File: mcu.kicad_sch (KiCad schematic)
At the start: 1 part, among them U2 ESP32-S3-WROOM-1

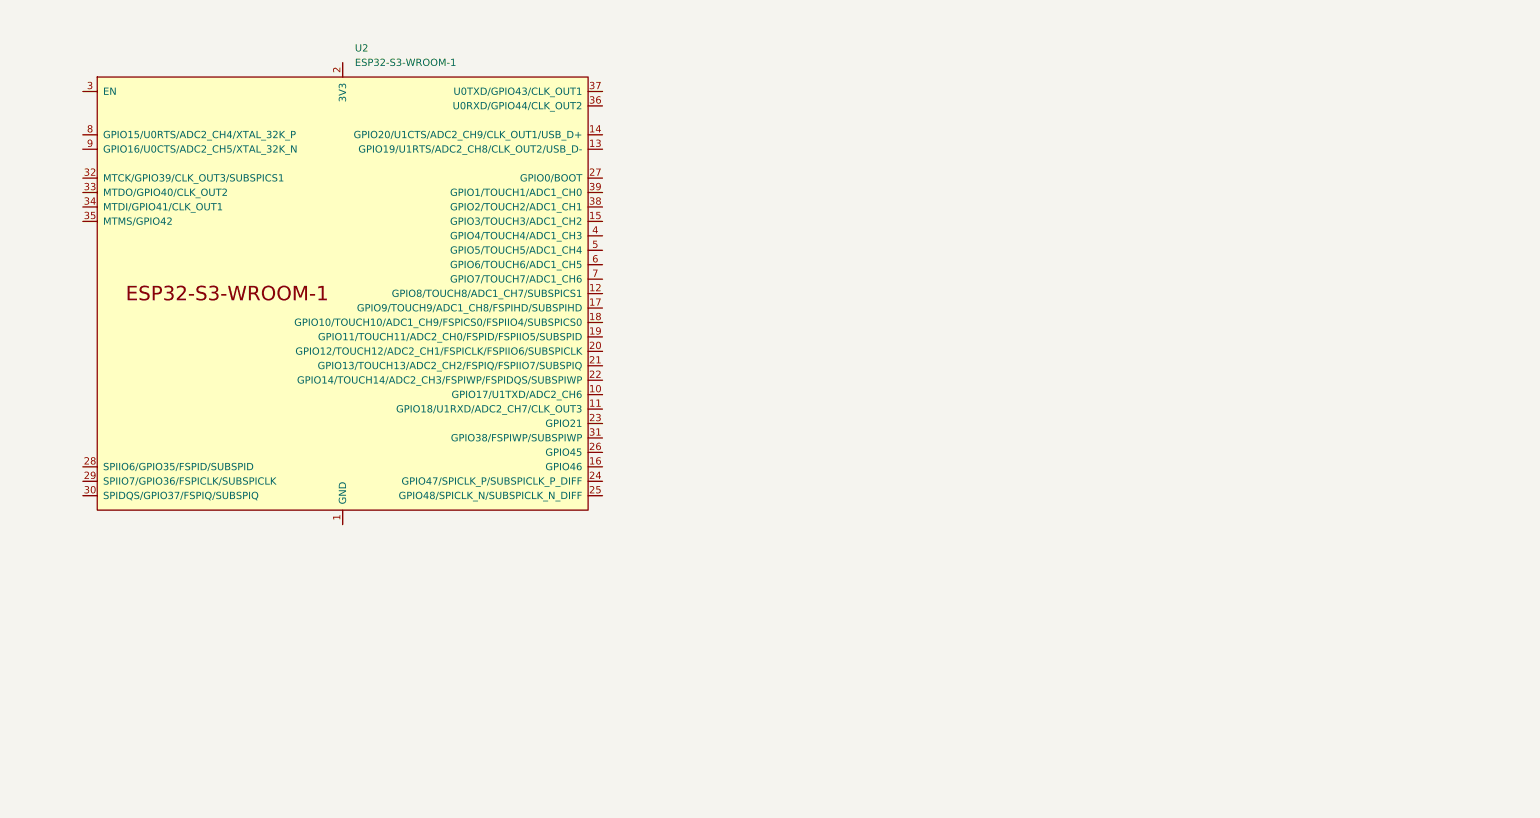
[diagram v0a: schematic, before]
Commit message: power sch. done, MCU powering as well
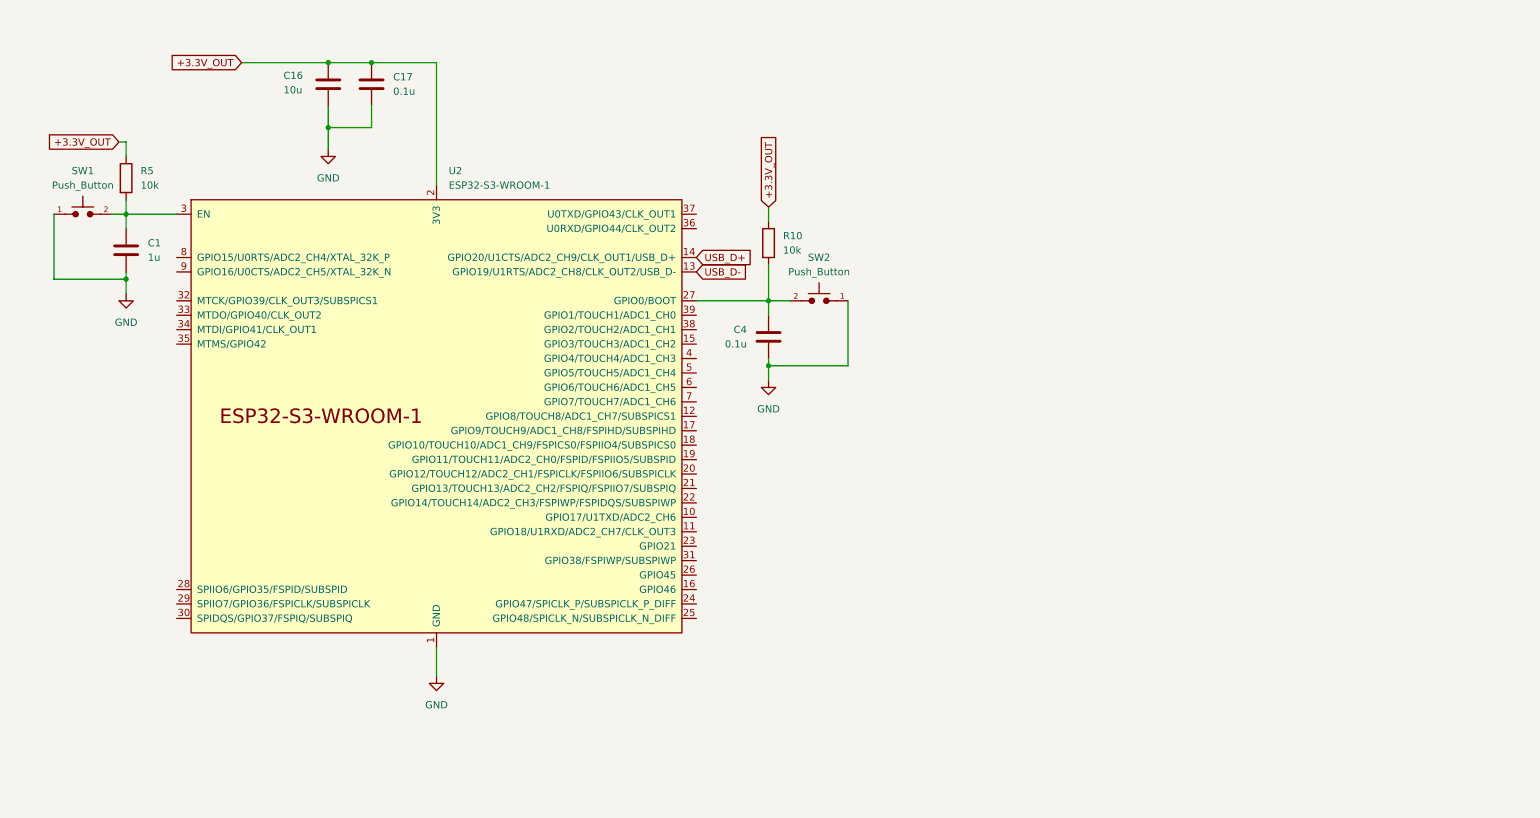
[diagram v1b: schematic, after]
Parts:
- added C1: 1u, symbol Device:C
- added C16: 10u, Capacitor_THT:C_Radial_D12.5mm_H25.0mm_P5.00mm, symbol Device:C
- added C17: 0.1u, Capacitor_THT:C_Radial_D12.5mm_H25.0mm_P5.00mm, symbol Device:C
- added C4: 0.1u, symbol Device:C
- added R10, R5: 10k, symbol Device:R
- added SW1, SW2: Push_Button, Button_Switch_THT:SW_PUSH_6mm, symbol PCM_SL_Devices:Push_Button
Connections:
- net GND: now reaches U2.1 (GND), U2.40 (GND), U2.41 (GND)
- net GND: now also C1.2, C16.2, C17.2, C4.2, SW1.1, SW2.1
- net USB_D-: now reaches U2.13 (GPIO19/U1RTS/ADC2_CH8/CLK_OUT2/USB_D-)
- net USB_D+: now reaches U2.14 (GPIO20/U1CTS/ADC2_CH9/CLK_OUT1/USB_D+)
- net +3.3V_OUT: now reaches U2.2 (3V3)
- net +3.3V_OUT: now also C16.1, C17.1, R10.1, R5.1
- net at U2.27 (GPIO0/BOOT): now also C4.1, R10.2, SW2.2
- net at U2.3 (EN): now also C1.1, R5.2, SW1.2
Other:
- moved on the sheet: U2

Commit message: Small ammendments
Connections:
- net IMU_CS: now reaches U2.18 (GPIO10/TOUCH10/ADC1_CH9/FSPICS0/FSPIIO4/SUBSPICS0)
- net IMU_MOSI: now reaches U2.19 (GPIO11/TOUCH11/ADC2_CH0/FSPID/FSPIIO5/SUBSPID)
- net IMU_SCK: now reaches U2.20 (GPIO12/TOUCH12/ADC2_CH1/FSPICLK/FSPIIO6/SUBSPICLK)
- net IMU_MISO: now reaches U2.21 (GPIO13/TOUCH13/ADC2_CH2/FSPIQ/FSPIIO7/SUBSPIQ)
- net BARO_CS: now reaches U2.22 (GPIO14/TOUCH14/ADC2_CH3/FSPIWP/FSPIDQS/SUBSPIWP)
- net ADC_C_SENSE: now reaches U2.38 (GPIO2/TOUCH2/ADC1_CH1)
- net ADC_V_SENSE: now reaches U2.39 (GPIO1/TOUCH1/ADC1_CH0)
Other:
- moved on the sheet: C4, R10, SW2
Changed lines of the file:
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@@
 	(paper "A4")
+	(junction
+		(at 156.21 67.31)
+		(diameter 0)
+		(color 0 0 0 0)
+	)
 	(junction
 		(at 76.2 25.4)
@@
 	)
 	(junction
-		(at 146.05 78.74)
+		(at 156.21 78.74)
 		(diameter 0)
 		(color 0 0 0 0)
@@
 	)
 	(junction
-		(at 146.05 67.31)
-		(diameter 0)
-		(color 0 0 0 0)
-	)
-	(junction
 		(at 68.58 36.83)
 		(diameter 0)
@@
 	(wire
 		(pts
+			(xy 146.05 78.74) (xy 146.05 81.28)
+		)
+		(stroke
+			(width 0)
+			(type default)
+		)
+	)
+	(wire
+		(pts
 			(xy 76.2 25.4) (xy 87.63 25.4)
 		)
@@
 	(wire
 		(pts
-			(xy 146.05 67.31) (xy 149.86 67.31)
+			(xy 156.21 67.31) (xy 161.29 67.31)
 		)
 		(stroke
@@
 	(wire
 		(pts
-			(xy 160.02 67.31) (xy 160.02 78.74)
+			(xy 171.45 67.31) (xy 171.45 78.74)
 		)
 		(stroke
@@
 	(wire
 		(pts
-			(xy 146.05 78.74) (xy 160.02 78.74)
+			(xy 146.05 78.74) (xy 156.21 78.74)
 		)
 		(stroke
@@
 	(wire
 		(pts
-			(xy 146.05 67.31) (xy 146.05 69.85)
+			(xy 156.21 67.31) (xy 156.21 69.85)
 		)
 		(stroke
@@
 	(wire
 		(pts
-			(xy 133.35 67.31) (xy 146.05 67.31)
+			(xy 133.35 67.31) (xy 156.21 67.31)
 		)
 		(stroke
@@
 	(wire
 		(pts
+			(xy 156.21 49.53) (xy 156.21 53.34)
+		)
+		(stroke
+			(width 0)
+			(type default)
+		)
+	)
+	(wire
+		(pts
 			(xy 33.02 49.53) (xy 33.02 54.61)
 		)
@@
 	(wire
 		(pts
-			(xy 146.05 50.8) (xy 146.05 53.34)
+			(xy 156.21 78.74) (xy 171.45 78.74)
 		)
 		(stroke
@@
 	(wire
 		(pts
-			(xy 146.05 60.96) (xy 146.05 67.31)
-		)
-		(stroke
-			(width 0)
-			(type default)
-		)
-	)
-	(wire
-		(pts
-			(xy 146.05 77.47) (xy 146.05 81.28)
-		)
-		(stroke
-			(width 0)
-			(type default)
+			(xy 156.21 60.96) (xy 156.21 67.31)
+		)
+		(stroke
+			(width 0)
+			(type default)
+		)
+	)
+	(wire
+		(pts
+			(xy 156.21 77.47) (xy 156.21 78.74)
+		)
+		(stroke
+			(width 0)
+			(type default)
+		)
+	)
+	(global_label "IMU_MOSI"
+		(shape input)
+		(at 133.35 95.25 0)
+		(fields_autoplaced yes)
+		(effects
+			(font
+				(size 1.27 1.27)
+			)
+			(justify left)
+		)
+		(property "Intersheetrefs" "${INTERSHEET_REFS}"
+			(at 145.2857 95.25 0)
+			(hide yes)
+			(show_name no)
+			(do_not_autoplace no)
+			(effects
+				(font
+					(size 1.27 1.27)
+				)
+				(justify left)
+			)
+		)
+	)
+	(global_label "IMU_CS"
+		(shape input)
+		(at 133.35 92.71 0)
+		(fields_autoplaced yes)
+		(effects
+			(font
+				(size 1.27 1.27)
+			)
+			(justify left)
+		)
+		(property "Intersheetrefs" "${INTERSHEET_REFS}"
+			(at 143.169 92.71 0)
+			(hide yes)
+			(show_name no)
+			(do_not_autoplace no)
+			(effects
+				(font
+					(size 1.27 1.27)
+				)
+				(justify left)
+			)
+		)
+	)
+	(global_label "ADC_C_SENSE"
+		(shape input)
+		(at 133.35 72.39 0)
+		(fields_autoplaced yes)
+		(effects
+			(font
+				(size 1.27 1.27)
+			)
+			(justify left)
+		)
+		(property "Intersheetrefs" "${INTERSHEET_REFS}"
+			(at 149.2165 72.39 0)
+			(hide yes)
+			(show_name no)
+			(do_not_autoplace no)
+			(effects
+				(font
+					(size 1.27 1.27)
+				)
+				(justify left)
+			)
 		)
 	)
@@
 		)
 	)
+	(global_label "BARO_CS"
+		(shape input)
+		(at 133.35 102.87 0)
+		(fields_autoplaced yes)
+		(effects
+			(font
+				(size 1.27 1.27)
+			)
+			(justify left)
+		)
+		(property "Intersheetrefs" "${INTERSHEET_REFS}"
+			(at 144.7414 102.87 0)
+			(hide yes)
+			(show_name no)
+			(do_not_autoplace no)
+			(effects
+				(font
+					(size 1.27 1.27)
+				)
+				(justify left)
+			)
+		)
+	)
+	(global_label "IMU_SCK"
+		(shape input)
+		(at 133.35 97.79 0)
+		(fields_autoplaced yes)
+		(effects
+			(font
+				(size 1.27 1.27)
+			)
+			(justify left)
+		)
+		(property "Intersheetrefs" "${INTERSHEET_REFS}"
+			(at 144.439 97.79 0)
+			(hide yes)
+			(show_name no)
+			(do_not_autoplace no)
+			(effects
+				(font
+					(size 1.27 1.27)
+				)
+				(justify left)
+			)
+		)
+	)
 	(global_label "+3.3V_OUT"
 		(shape input)
@@
 		)
 	)
-	(global_label "+3.3V_OUT"
+	(global_label "IMU_MISO"
 		(shape input)
-		(at 146.05 50.8 90)
+		(at 133.35 100.33 0)
 		(fields_autoplaced yes)
 		(effects
@@
 		)
 		(property "Intersheetrefs" "${INTERSHEET_REFS}"
-			(at 146.05 37.5338 90)
+			(at 145.2857 100.33 0)
+			(hide yes)
+			(show_name no)
+			(do_not_autoplace no)
+			(effects
+				(font
+					(size 1.27 1.27)
+				)
+				(justify left)
+			)
+		)
+	)
+	(global_label "+3.3V_OUT"
+		(shape input)
+		(at 156.21 49.53 90)
+		(fields_autoplaced yes)
+		(effects
+			(font
+				(size 1.27 1.27)
+			)
+			(justify left)
+		)
+		(property "Intersheetrefs" "${INTERSHEET_REFS}"
+			(at 156.21 36.2638 90)
+			(hide yes)
+			(show_name no)
+			(do_not_autoplace no)
+			(effects
+				(font
+					(size 1.27 1.27)
+				)
+				(justify left)
+			)
+		)
+	)
+	(global_label "ADC_V_SENSE"
+		(shape input)
+		(at 133.35 69.85 0)
+		(fields_autoplaced yes)
+		(effects
+			(font
+				(size 1.27 1.27)
+			)
+			(justify left)
+		)
+		(property "Intersheetrefs" "${INTERSHEET_REFS}"
+			(at 149.0351 69.85 0)
 			(hide yes)
 			(show_name no)
@@
 	(symbol
 		(lib_id "PCM_SL_Devices:Push_Button")
-		(at 154.94 67.31 0)
+		(at 166.37 67.31 0)
 		(mirror y)
 		(unit 1)
@@
 		(fields_autoplaced yes)
 		(property "Reference" "SW2"
-			(at 154.94 59.69 0)
+			(at 166.37 59.69 0)
 			(show_name no)
 			(do_not_autoplace no)
@@
 		)
 		(property "Value" "Push_Button"
-			(at 154.94 62.23 0)
+			(at 166.37 62.23 0)
 			(show_name no)
 			(do_not_autoplace no)
@@
 		)
 		(property "Footprint" "Button_Switch_THT:SW_PUSH_6mm"
-			(at 155.067 70.485 0)
+			(at 166.497 70.485 0)
 			(hide yes)
 			(show_name no)
@@
 		)
 		(property "Datasheet" ""
-			(at 154.94 67.31 0)
+			(at 166.37 67.31 0)
 			(hide yes)
 			(show_name no)
@@
 		)
 		(property "Description" "Common 6mmx6mm Push Button"
-			(at 154.94 67.31 0)
+			(at 166.37 67.31 0)
 			(hide yes)
 			(show_name no)
@@
 	(symbol
 		(lib_id "Device:C")
-		(at 146.05 73.66 0)
+		(at 156.21 73.66 0)
 		(mirror y)
 		(unit 1)
@@
 		(fields_autoplaced yes)
 		(property "Reference" "C4"
-			(at 142.24 72.3899 0)
+			(at 152.4 72.3899 0)
 			(show_name no)
 			(do_not_autoplace no)
@@
 		)
 		(property "Value" "0.1u"
-			(at 142.24 74.9299 0)
+			(at 152.4 74.9299 0)
 			(show_name no)
 			(do_not_autoplace no)
@@
 		)
 		(property "Footprint" ""
-			(at 145.0848 77.47 0)
+			(at 155.2448 77.47 0)
 			(hide yes)
 			(show_name no)
@@
 		)
 		(property "Datasheet" ""
-			(at 146.05 73.66 0)
+			(at 156.21 73.66 0)
 			(hide yes)
 			(show_name no)
@@
 		)
 		(property "Description" "Unpolarized capacitor"
-			(at 146.05 73.66 0)
+			(at 156.21 73.66 0)
 			(hide yes)
 			(show_name no)
@@
 	(symbol
 		(lib_id "Device:R")
-		(at 146.05 57.15 0)
+		(at 156.21 57.15 0)
 		(unit 1)
 		(body_style 1)
@@
 		(fields_autoplaced yes)
 		(property "Reference" "R10"
-			(at 148.59 55.8799 0)
+			(at 158.75 55.8799 0)
 			(show_name no)
 			(do_not_autoplace no)
@@
 		)
 		(property "Value" "10k"
-			(at 148.59 58.4199 0)
+			(at 158.75 58.4199 0)
 			(show_name no)
 			(do_not_autoplace no)
@@
 		)
 		(property "Footprint" ""
-			(at 144.272 57.15 90)
+			(at 154.432 57.15 90)
 			(hide yes)
 			(show_name no)
@@
 		)
 		(property "Datasheet" ""
-			(at 146.05 57.15 0)
+			(at 156.21 57.15 0)
 			(hide yes)
 			(show_name no)
@@
 		)
 		(property "Description" "Resistor"
-			(at 146.05 57.15 0)
-			(hide yes)
-			(show_name no)
+			(at 156.21 57.15 0)
+			(hide yes)
+			(show_name no)

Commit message: 8.09.2026 - 19:33
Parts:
- added J10: M3, Connector_PinHeader_2.54mm:PinHeader_1x03_P2.54mm_Horizontal, symbol Connector_Generic:Conn_01x03
- added J7: M0, Connector_PinHeader_2.54mm:PinHeader_1x03_P2.54mm_Horizontal, symbol Connector_Generic:Conn_01x03
- added J8: M1, Connector_PinHeader_2.54mm:PinHeader_1x03_P2.54mm_Horizontal, symbol Connector_Generic:Conn_01x03
- added J9: M2, Connector_PinHeader_2.54mm:PinHeader_1x03_P2.54mm_Horizontal, symbol Connector_Generic:Conn_01x03
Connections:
- net GND: now also J10.3 (Pin_3), J7.3 (Pin_3), J8.3 (Pin_3), J9.3 (Pin_3)
- net M0: now reaches U2.32 (MTCK/GPIO39/CLK_OUT3/SUBSPICS1)
- net M0: now also J7.1 (Pin_1)
- net M1: now reaches U2.33 (MTDO/GPIO40/CLK_OUT2)
- net M1: now also J8.1 (Pin_1)
- net M2: now reaches U2.34 (MTDI/GPIO41/CLK_OUT1)
- net M2: now also J9.1 (Pin_1)
- net M3: now reaches U2.35 (MTMS/GPIO42)
- net M3: now also J10.1 (Pin_1)
- no-connect marks 0 -> 4
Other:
- note added: "MOTORS"

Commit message: 8.09.2026 - 20:26
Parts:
- added J11: Conn_01x10, Connector_JST:JST_GH_BM10B-GHS-TBT_1x10-1MP_P1.25mm_Vertical, symbol Connector_Generic:Conn_01x10
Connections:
- net GND: now also J11.10 (Pin_10)
- net GPS_RX: now reaches U2.10 (GPIO17/U1TXD/ADC2_CH6)
- net GPS_RX: now also J11.2 (Pin_2)
- net GPS_TX: now reaches U2.11 (GPIO18/U1RXD/ADC2_CH7/CLK_OUT3)
- net GPS_TX: now also J11.3 (Pin_3)
- net GPS_SDA: now reaches U2.12 (GPIO8/TOUCH8/ADC1_CH7/SUBSPICS1)
- net GPS_SDA: now also J11.5 (Pin_5)
- net GPS_SCL: now reaches U2.17 (GPIO9/TOUCH9/ADC1_CH8/FSPIHD/SUBSPIHD)
- net GPS_SCL: now also J11.4 (Pin_4)
- net GPS_BUZZ: now reaches U2.5 (GPIO5/TOUCH5/ADC1_CH4)
- net GPS_BUZZ: now also J11.9 (Pin_9)
- new net +5V_OUT: J11.1 (Pin_1)
- no-connect marks 4 -> 7

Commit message: 8.09.2026 - 23:26
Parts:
- added J12: Conn_01x03, symbol Connector_Generic:Conn_01x03
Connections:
- net +5V_OUT: now also J12.2 (Pin_2)
- net GND: now also J12.3 (Pin_3)
- net SBUS: now reaches U2.9 (GPIO16/U0CTS/ADC2_CH5/XTAL_32K_N)
- net SBUS: now also J12.1 (Pin_1)
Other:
- note added: "GPS"
- note added: "RC"
- moved on the sheet: C1, C16, C17, C4, J11, R10, R5, SW1, SW2, U2

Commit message: 9.09.2026 - 00:22
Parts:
- added C29: 100n, symbol Device:C
- added R17: 110, symbol Device:R
- added R18: 10k, symbol Device:R
- added R19: 330, symbol Device:R
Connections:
- net +3.3V_OUT: now also J11.8 (Pin_8), R18.1
- net GND: now also C29.2
- net GPS_BUZZ: now also R17.1; no longer U2.5 (GPIO5/TOUCH5/ADC1_CH4)
- net GPS_SFT_SWT: now reaches U2.23 (GPIO21)
- net GPS_SFT_SWT: now also J11.6 (Pin_6), C29.1, R18.2
- net at U2.24 (GPIO47/SPICLK_P/SUBSPICLK_P_DIFF): now also R19.2
- net GPS_LED: now reaches J11.7 (Pin_7)
- net GPS_LED: now also R19.1
- new net: R17.2, U2.5 (GPIO5/TOUCH5/ADC1_CH4)
- no-connect marks 7 -> 4
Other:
- moved on the sheet: C4, J11, R10, SW2
